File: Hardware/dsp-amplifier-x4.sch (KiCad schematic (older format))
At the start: 63 parts, among them J1 USBi, J2 EXT, J3 Raspberry_Pi_2_3, J4 Screw_Terminal_01x02, J5 Screw_Terminal_01x02, J6 Screw_Terminal_01x02, J7 Screw_Terminal_01x02, P1 Conn_WallPlug, Q1 STD2805, U1 ADAU1452, U2 TSOP583xx

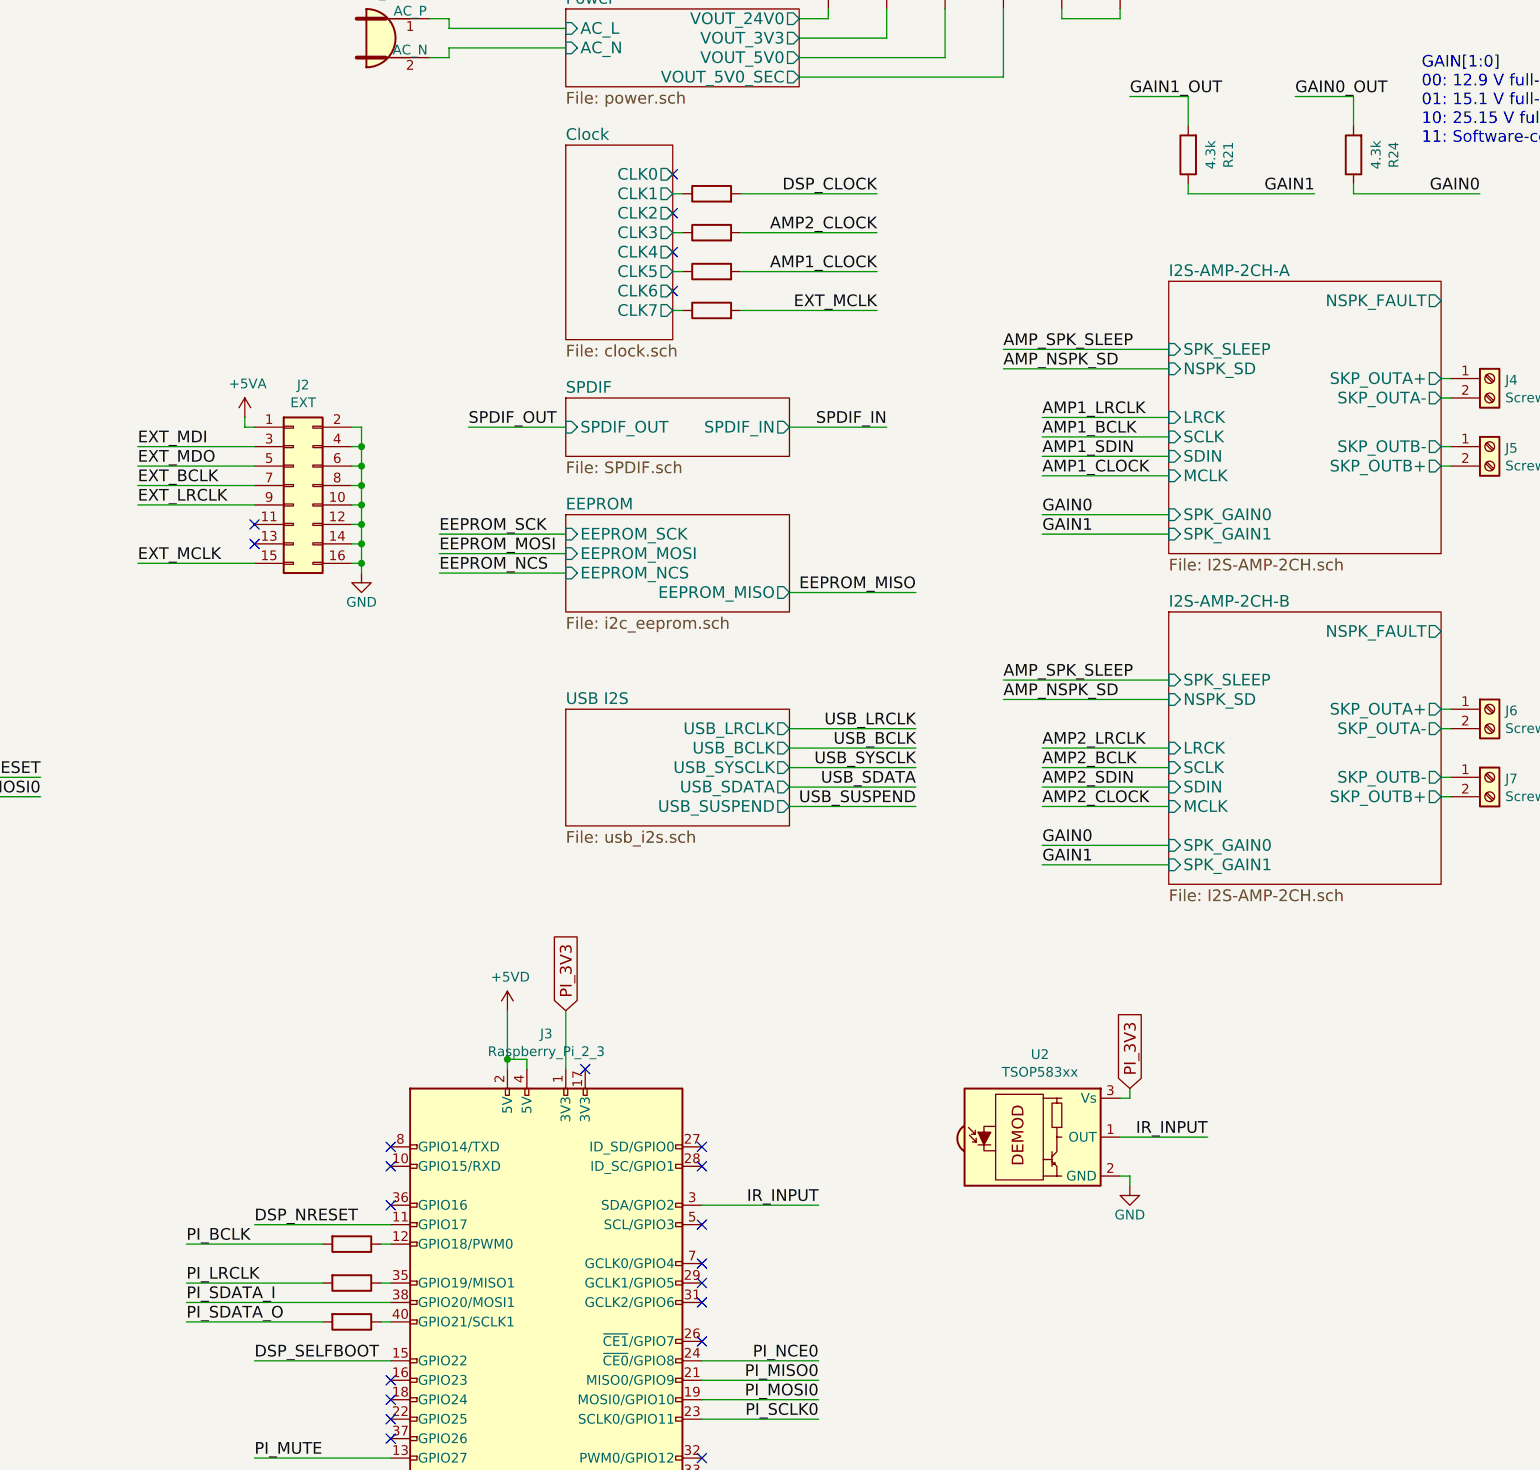
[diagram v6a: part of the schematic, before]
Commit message: connect pi i2c to header
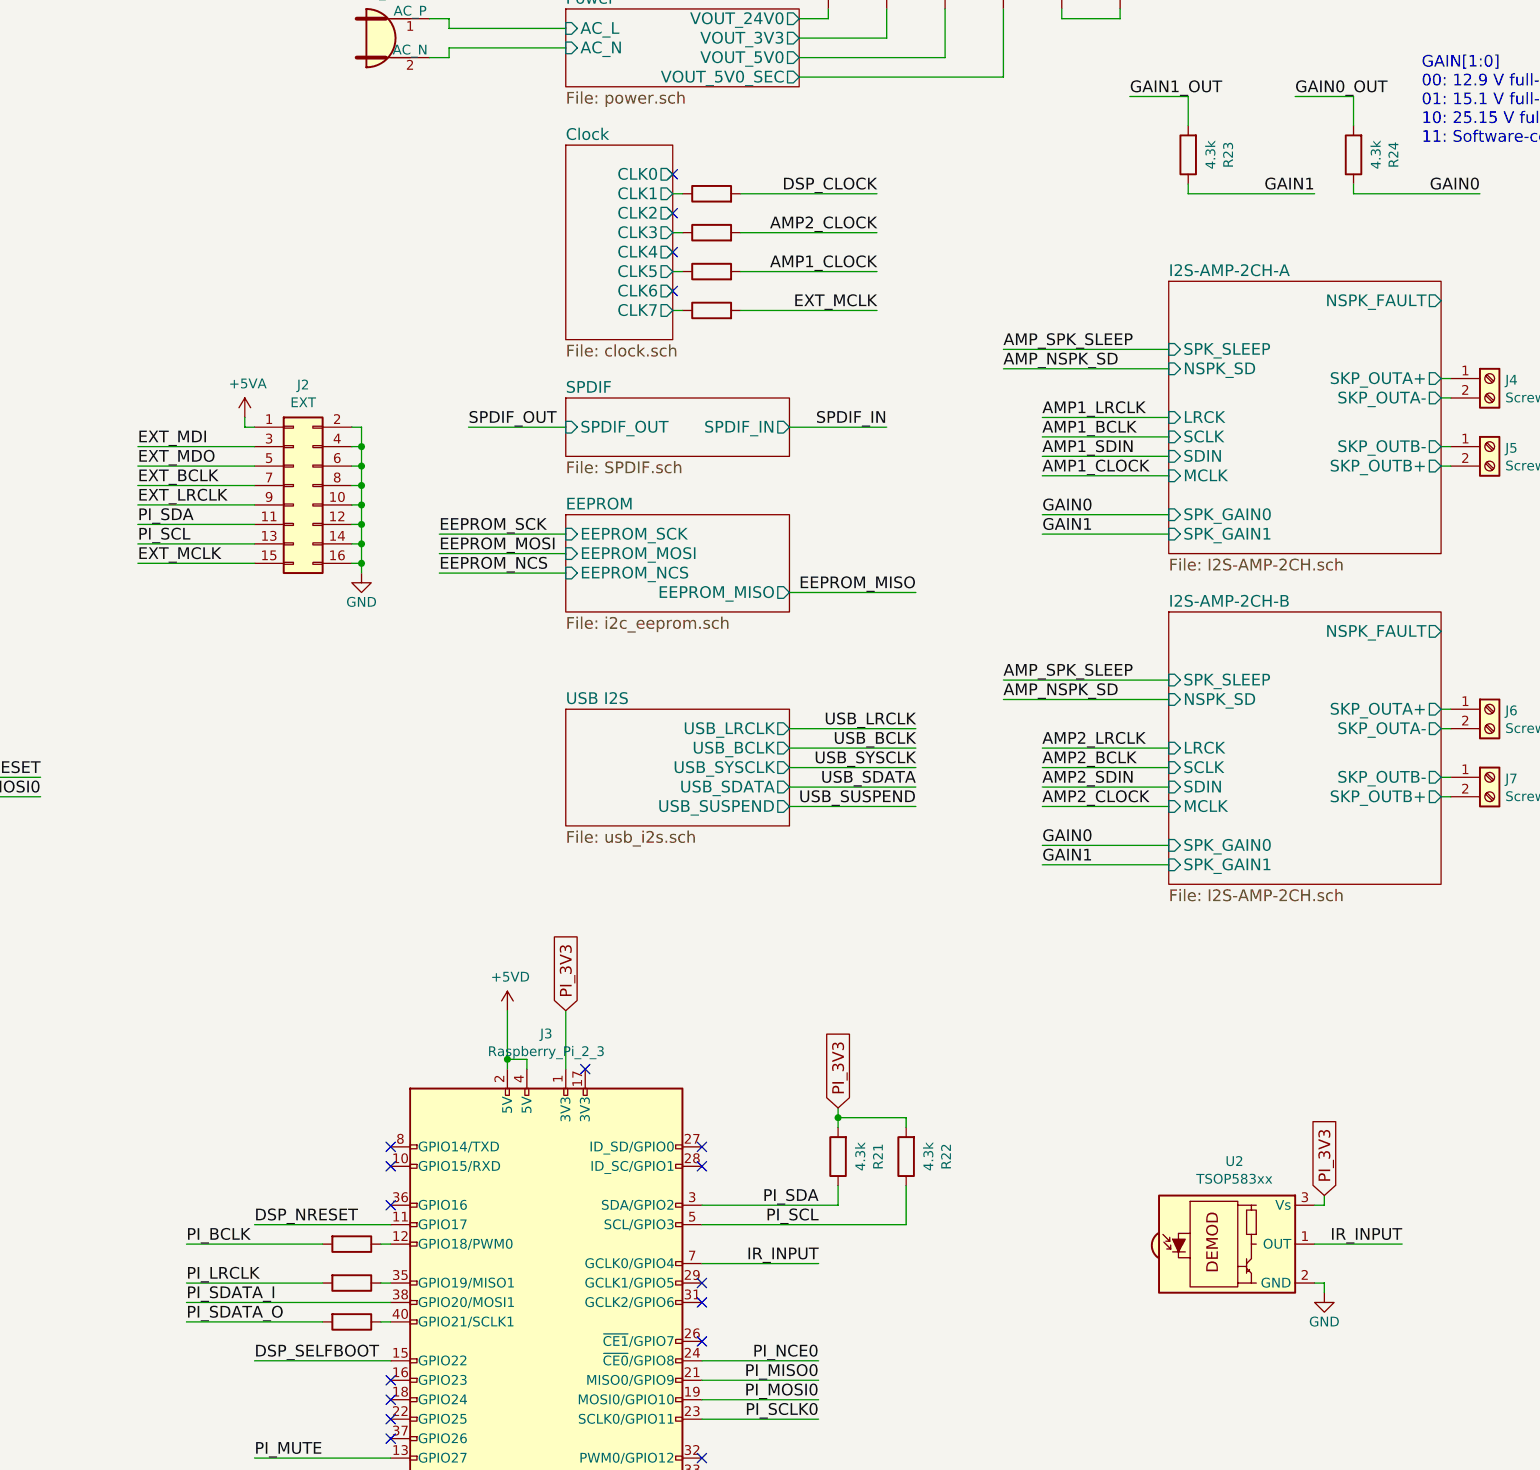
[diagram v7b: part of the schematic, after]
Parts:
- added R21, R22: 4.3k, Resistor_SMD:R_0603_1608Metric_Pad0.98x0.95mm_HandSolder, symbol Device:R
- renumbered R21 to R23
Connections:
- net IR_INPUT: now also J3.7 (GCLK0/GPIO4); no longer J3.3 (SDA/GPIO2)
- net PI_3V3: now also R21.2, R22.2
- net PI_SDA: now reaches J2.11 (Pin_11)
- net PI_SDA: now also J3.3 (SDA/GPIO2), R21.1
- net PI_SCL: now reaches J2.13 (Pin_13)
- net PI_SCL: now also J3.5 (SCL/GPIO3), R22.1
- no-connect marks 39 -> 35
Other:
- moved on the sheet: U2
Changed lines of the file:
@@
 NoConn ~ 6600 4650
 $Comp
-L power:GND #PWR022
+L power:GND #PWR023
 U 1 1 611E8646
 P 6650 5100
-F 0 "#PWR022" H 6650 4850 50  0001 C CNN
+F 0 "#PWR023" H 6650 4850 50  0001 C CNN
 F 1 "GND" H 6650 4950 50  0000 C CNN
 F 2 "" H 6650 5100 50  0001 C CNN
@@
 $EndComp
 $Comp
-L power:GND #PWR018
+L power:GND #PWR019
 U 1 1 6186C217
 P 4950 6950
-F 0 "#PWR018" H 4950 6700 50  0001 C CNN
+F 0 "#PWR019" H 4950 6700 50  0001 C CNN
 F 1 "GND" H 4950 6800 50  0000 C CNN
 F 2 "" H 4950 6950 50  0001 C CNN
@@
 $EndComp
 $Comp
-L power:GND #PWR019
+L power:GND #PWR020
 U 1 1 6186CD72
 P 5300 6950
-F 0 "#PWR019" H 5300 6700 50  0001 C CNN
+F 0 "#PWR020" H 5300 6700 50  0001 C CNN
 F 1 "GND" H 5300 6800 50  0000 C CNN
 F 2 "" H 5300 6950 50  0001 C CNN
@@
 $EndComp
 $Comp
-L power:GND #PWR020
+L power:GND #PWR021
 U 1 1 618F742F
 P 5650 7300
-F 0 "#PWR020" H 5650 7050 50  0001 C CNN
+F 0 "#PWR021" H 5650 7050 50  0001 C CNN
 F 1 "GND" H 5650 7150 50  0000 C CNN
 F 2 "" H 5650 7300 50  0001 C CNN
@@
 	13150 1850 13800 1850
 $Comp
-L Device:R R21
+L Device:R R23
 U 1 1 60E78271
 P 13150 1650
-F 0 "R21" V 12943 1650 50  0000 C CNN
+F 0 "R23" V 12943 1650 50  0000 C CNN
 F 1 "4.3k" V 13034 1650 50  0000 C CNN
 F 2 "Resistor_SMD:R_0603_1608Metric_Pad0.98x0.95mm_HandSolder" V 13080 1650 50  0001 C CNN
@@
 NoConn ~ 9050 6750
 NoConn ~ 9050 6850
-NoConn ~ 10650 7350
 NoConn ~ 10650 7450
 NoConn ~ 10650 7550
@@
 NoConn ~ 10650 8450
 NoConn ~ 10650 7750
-NoConn ~ 10650 7150
 $Sheet
 S 9950 3500 1150 500
@@
 NoConn ~ 6100 4650
 NoConn ~ 6100 4750
-NoConn ~ 8350 3550
-NoConn ~ 8350 3650
 Wire Wire Line
 	5300 4850 4400 4850
@@
 L Interface_Optical:TSOP583xx U2
 U 1 1 60970E2B
-P 12400 6700
-F 0 "U2" H 12388 7125 50  0000 C CNN
-F 1 "TSOP583xx" H 12388 7034 50  0000 C CNN
-F 2 "OptoDevice:Vishay_MINICAST-3Pin" H 12350 6325 50  0001 C CNN
-F 3 "http://www.vishay.com/docs/82462/tsop581.pdf" H 13050 7000 50  0001 C CNN
-	1    12400 6700
+P 13400 7250
+F 0 "U2" H 13388 7675 50  0000 C CNN
+F 1 "TSOP583xx" H 13388 7584 50  0000 C CNN
+F 2 "OptoDevice:Vishay_MINICAST-3Pin" H 13350 6875 50  0001 C CNN
+F 3 "http://www.vishay.com/docs/82462/tsop581.pdf" H 14050 7550 50  0001 C CNN
+	1    13400 7250
 	1    0    0    -1
 $EndComp
@@
 L power:GND #PWR034
 U 1 1 60978480
-P 12850 6950
-F 0 "#PWR034" H 12850 6700 50  0001 C CNN
-F 1 "GND" H 12850 6800 50  0000 C CNN
-F 2 "" H 12850 6950 50  0001 C CNN
-F 3 "" H 12850 6950 50  0001 C CNN
-	1    12850 6950
-	1    0    0    -1
-$EndComp
-Wire Wire Line
-	12800 6900 12850 6900
-Wire Wire Line
-	12850 6900 12850 6950
-Text Label 11250 7050 2    60   ~ 0
+P 13850 7500
+F 0 "#PWR034" H 13850 7250 50  0001 C CNN
+F 1 "GND" H 13850 7350 50  0000 C CNN
+F 2 "" H 13850 7500 50  0001 C CNN
+F 3 "" H 13850 7500 50  0001 C CNN
+	1    13850 7500
+	1    0    0    -1
+$EndComp
+Wire Wire Line
+	13800 7450 13850 7450
+Wire Wire Line
+	13850 7450 13850 7500
+Text Label 11250 7350 2    60   ~ 0
 IR_INPUT
-Text Label 13250 6700 2    60   ~ 0
+Text Label 14250 7250 2    60   ~ 0
 IR_INPUT
 Wire Wire Line
-	13250 6700 12800 6700
+	14250 7250 13800 7250
 Wire Wire Line
 	9950 6050 9950 6350
 Text GLabel 9950 6050 1    60   Input ~ 0
 PI_3V3
-Text GLabel 12850 6450 1    60   Input ~ 0
+Text GLabel 13850 7000 1    60   Input ~ 0
 PI_3V3
 Wire Wire Line
-	12850 6450 12850 6500
-Wire Wire Line
-	12850 6500 12800 6500
+	13850 7000 13850 7050
+Wire Wire Line
+	13850 7050 13800 7050
 NoConn ~ 9050 7950
 Text Label 11750 5000 2    60   ~ 0
@@
 	11250 8150 10650 8150
 Wire Wire Line
-	11250 7050 10650 7050
+	11250 7350 10650 7350
 NoConn ~ 4400 2350
 $Comp
-L power:+5VA #PWR0116
+L power:+5VA #PWR024
 U 1 1 609E250E
 P 8300 3000
-F 0 "#PWR0116" H 8300 2850 50  0001 C CNN
+F 0 "#PWR024" H 8300 2850 50  0001 C CNN
 F 1 "+5VA" H 8315 3173 50  0000 C CNN
 F 2 "" H 8300 3000 50  0001 C CNN
@@
 	5950 1450 5950 1400
 $Comp
-L power:GND #PWR023
+L power:GND #PWR022
 U 1 1 608051CA
 P 5950 1450
-F 0 "#PWR023" H 5950 1200 50  0001 C CNN
+F 0 "#PWR022" H 5950 1200 50  0001 C CNN
 F 1 "GND" H 5950 1300 50  0000 C CNN
 F 2 "" H 5950 1450 50  0001 C CNN
@@
 	4950 1400 4950 1450
 $Comp
-L power:GND #PWR021
+L power:GND #PWR018
 U 1 1 607F06EF
 P 4950 1450
-F 0 "#PWR021" H 4950 1200 50  0001 C CNN
+F 0 "#PWR018" H 4950 1200 50  0001 C CNN
 F 1 "GND" H 4950 1300 50  0000 C CNN
 F 2 "" H 4950 1450 50  0001 C CNN
@@
 Wire Wire Line
 	4400 2850 5400 2850
+Text Label 11250 7050 2    60   ~ 0
+PI_SDA
+Text Label 11250 7150 2    60   ~ 0
+PI_SCL
+Text Label 7750 3550 0    60   ~ 0
+PI_SDA
+Text Label 7750 3650 0    60   ~ 0
+PI_SCL
+Wire Wire Line
+	7750 3550 8350 3550
+Wire Wire Line
+	8350 3650 7750 3650
+$Comp
+L Device:R R21
+U 1 1 60CDE4BC
+P 11350 6800
+F 0 "R21" V 11143 6800 50  0000 C CNN
+F 1 "4.3k" V 11234 6800 50  0000 C CNN
+F 2 "Resistor_SMD:R_0603_1608Metric_Pad0.98x0.95mm_HandSolder" V 11280 6800 50  0001 C CNN
+F 3 "~" H 11350 6800 50  0001 C CNN
+	1    11350 6800
+	-1   0    0    1
+$EndComp
+$Comp
+L Device:R R22
+U 1 1 60CDF324
+P 11700 6800
+F 0 "R22" V 11493 6800 50  0000 C CNN
+F 1 "4.3k" V 11584 6800 50  0000 C CNN
+F 2 "Resistor_SMD:R_0603_1608Metric_Pad0.98x0.95mm_HandSolder" V 11630 6800 50  0001 C CNN
+F 3 "~" H 11700 6800 50  0001 C CNN
+	1    11700 6800
+	-1   0    0    1
+$EndComp
+Wire Wire Line
+	11350 7050 11350 6950
+Wire Wire Line
+	10650 7050 11350 7050
+Wire Wire Line
+	11700 7150 11700 6950
+Wire Wire Line
+	10650 7150 11700 7150
+Text GLabel 11350 6550 1    60   Input ~ 0
+PI_3V3
+Wire Wire Line
+	11350 6550 11350 6600
+Wire Wire Line
+	11350 6600 11700 6600
+Wire Wire Line
+	11700 6600 11700 6650
+Connection ~ 11350 6600
+Wire Wire Line
+	11350 6600 11350 6650
 $EndSCHEMATC

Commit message: fixes to plug placement
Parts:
- J1: footprint Connector_PinHeader_2.54mm:PinHeader_2x05_P2.54mm_Vertical -> Connector_IDC:IDC-Header_2x05_P2.54mm_Vertical
- J2: footprint Connector_PinHeader_2.54mm:PinHeader_2x08_P2.54mm_Vertical -> Connector_IDC:IDC-Header_2x08_P2.54mm_Vertical
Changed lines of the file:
@@
 F 0 "J1" H 6350 5267 50  0000 C CNN
 F 1 "USBi" H 6350 5176 50  0000 C CNN
-F 2 "Connector_PinHeader_2.54mm:PinHeader_2x05_P2.54mm_Vertical" H 6300 4850 50  0001 C CNN
+F 2 "Connector_IDC:IDC-Header_2x05_P2.54mm_Vertical" H 6300 4850 50  0001 C CNN
 F 3 "~" H 6300 4850 50  0001 C CNN
 	1    6300 4850
@@
 F 0 "J2" H 8600 3867 50  0000 C CNN
 F 1 "EXT" H 8600 3776 50  0000 C CNN
-F 2 "Connector_PinHeader_2.54mm:PinHeader_2x08_P2.54mm_Vertical" H 8550 3350 50  0001 C CNN
+F 2 "Connector_IDC:IDC-Header_2x08_P2.54mm_Vertical" H 8550 3350 50  0001 C CNN
 F 3 "~" H 8550 3350 50  0001 C CNN
 	1    8550 3350
@@
 Wire Wire Line
 	14000 1800 14000 1850
-Text Label 13700 1350 0    60   ~ 0
+Text Label 13500 1350 0    60   ~ 0
 GAIN0_OUT
-Text Label 12850 1350 0    60   ~ 0
+Text Label 12650 1350 0    60   ~ 0
 GAIN1_OUT
 Wire Wire Line
-	12850 1350 13150 1350
-Wire Wire Line
 	13150 1350 13150 1500
-Wire Wire Line
-	13700 1350 14000 1350
 Wire Wire Line
 	14000 1350 14000 1500
@@
 Wire Wire Line
 	11350 6600 11350 6650
+Wire Wire Line
+	12650 1350 13150 1350
+Wire Wire Line
+	13500 1350 14000 1350
 $EndSCHEMATC
